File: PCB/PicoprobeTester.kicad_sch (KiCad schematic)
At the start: 10 parts, among them J1 External_Connections, J2 SWD, SW1 UART, SW2 Reset_Target

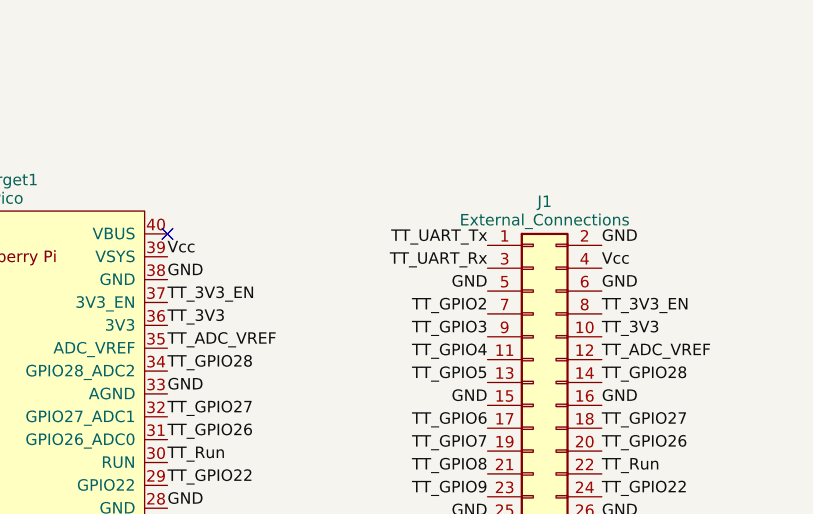
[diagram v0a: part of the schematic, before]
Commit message: Connected VBus and added text
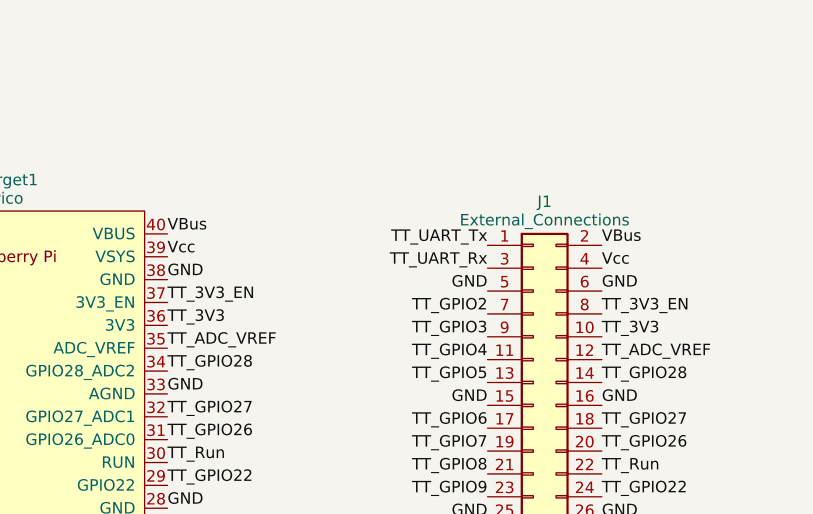
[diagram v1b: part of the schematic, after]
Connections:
- net GND: no longer J1.2 (Pin_2)
- net VBus: now reaches Target1.40 (VBUS)
- net VBus: now also J1.2 (Pin_2)
- no-connect marks 26 -> 25
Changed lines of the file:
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@@
   (no_connect (at 87.63 64.77))
   (no_connect (at 52.07 41.91))
-  (no_connect (at 162.56 43.18))
   (no_connect (at 52.07 82.55))
   (no_connect (at 52.07 64.77))
@@
     (effects (font (size 1.27 1.27)) (justify right bottom))
   )
+  (label "VBus" (at 210.82 44.45 0) (fields_autoplaced)
+    (effects (font (size 1.27 1.27)) (justify left bottom))
+  )
   (label "TT_GPIO10" (at 198.12 77.47 180) (fields_autoplaced)
     (effects (font (size 1.27 1.27)) (justify right bottom))
@@
     (effects (font (size 1.27 1.27)) (justify right bottom))
   )
-  (label "GND" (at 210.82 44.45 0) (fields_autoplaced)
-    (effects (font (size 1.27 1.27)) (justify left bottom))
-  )
   (label "GND" (at 162.56 48.26 0) (fields_autoplaced)
     (effects (font (size 1.27 1.27)) (justify left bottom))
   )
+  (label "VBus" (at 162.56 43.18 0) (fields_autoplaced)
+    (effects (font (size 1.27 1.27)) (justify left bottom))
+  )
